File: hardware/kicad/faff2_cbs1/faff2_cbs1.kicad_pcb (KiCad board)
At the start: 4 copper layers, 210 x 130 mm, 412 parts, among them J1001 USB_C_Receptacle_USB2.0_16P, J1002 TSW-105-07-F-D, J1003 SAMTEC_SHF-107-01-L-D-SM, J1101 1x6 2.54mm, J1102 1x6 2.54mm, J1103 Micro-Fit 1x3, J201 KPJX-4S, J301 PH1-06-UA, J501 1729076, J502 8510-4500PL, J503 CONUFL001-SMD, J504 CONUFL001-SMD, J601 FH12-10S-0.5SH(55), J602 FTSH-105-01-L-DV-K-TR, J603 8510-4500PL, J701 1752120, J702 1752120, J703 8510-4500PL, J901 BTN EXT, J902 SMA Jack, J903 J-LIM, Q1101 BSZ099N06LS5, Q1102 BSZ099N06LS5, Q1103 BSZ099N06LS5, Q1104 BSZ099N06LS5, Q1105 BSZ099N06LS5, Q1106 BSZ099N06LS5, Q201 DMP6023LFG-7, SW1001 PTS526, SW901 PTS526, SW902 PTS526, SW903 PTS526, SW904 PTS526, U1001 STM32H723VET6, U1002 USB3320C, U1003 SRAM 32Mb, U1004 MIC5365-1.8, U1101 DRV8323S, U301 LMR33630, U302 ADPL42005, U303 ADPL42005, U304 LMR33630, U501 ADS1235, U601 AM26LV32, U701 ADS1120, U801 24FC16T-I/OT, U901 SN74LVC1G17, U902 SN74LVC1G11, Y1001 24MHz, Y1002 24MHz 18pF

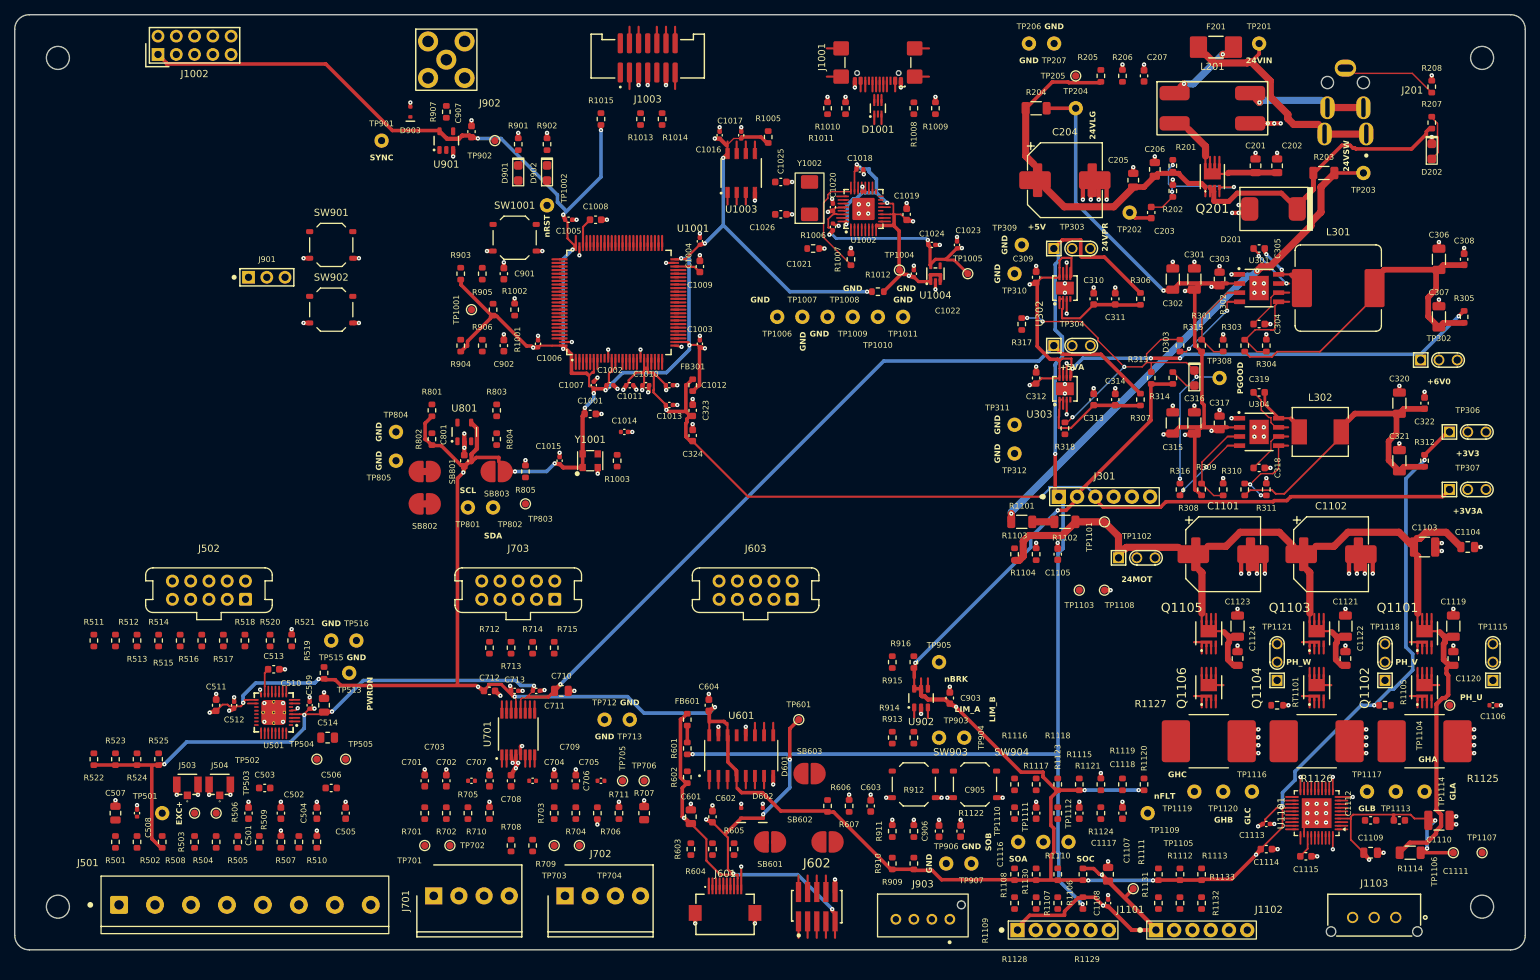
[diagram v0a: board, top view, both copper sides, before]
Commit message: pcb: routing step 4b/4c - via budget, and the three sealed pins (wip)
Step 4b: no power layer change may depend on too few barrels.  The test is
not how many vias a net has but how many it *depends* on -- a via whose
removal splits the net carries everything that crosses there -- so
`tools/route4b_powervias.py` searches every cut below the net's budget
(`ceil(I / 1.0 A)`, minimum 2 on a layer change) and parallels the vias it
names, tied on **both** outer layers, because two vias joined on one layer
only are in series through the other.  61 vias added over four passes;
`route_check.py --power` now returns ALL PROOFS PASS.

Step 4c (`tools/route4c_widen.py`, not yet run): the same argument for trace
width.  `connect_net`'s width ladder is right for the last hop onto a 0.5 mm
pad and wrong for a segment the whole rail crosses.

`tools/route_ripup.py`: windowed rip-up and reroute, for the three pins step 4
could not reach -- all three sealed in by another net's copper, which is the
R3-1 hazard.  Deletion runs in a child interpreter (Remove() poisons SWIG for
the rest of the process).  Two things had to be learned:

  * the pin-escape *reservation* is itself what seals a sealed pin -- leaving
    the package means crossing a neighbour's held lane at right angles, so
    U302 pin 7 routes in 14 mm with reservations off and not at all with them
    on; and the fan-out pass must not re-stub the ripped net's pins until the
    sealed net has its lane.
  * two adjacent pins that both have to leave the same way cannot both win on
    one layer.  U1101 pins 4/5 (VM and VDRAIN) cross layers instead; U302/U303
    PGOOD, the inner of its pair and a slow open-drain line, is the one that
    dives under the +6V0 approach.

U1101 pins 4 and 5 are done.  U302/U303 PGOOD are routed and the +6V0 tie is
mid-reroute -- banked here rather than held.

Also `tools/route7_stitch.py`, the G5 return-via pass, to run after the fill.

Co-Authored-By: Claude Opus 5 <noreply@anthropic.com>
Claude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
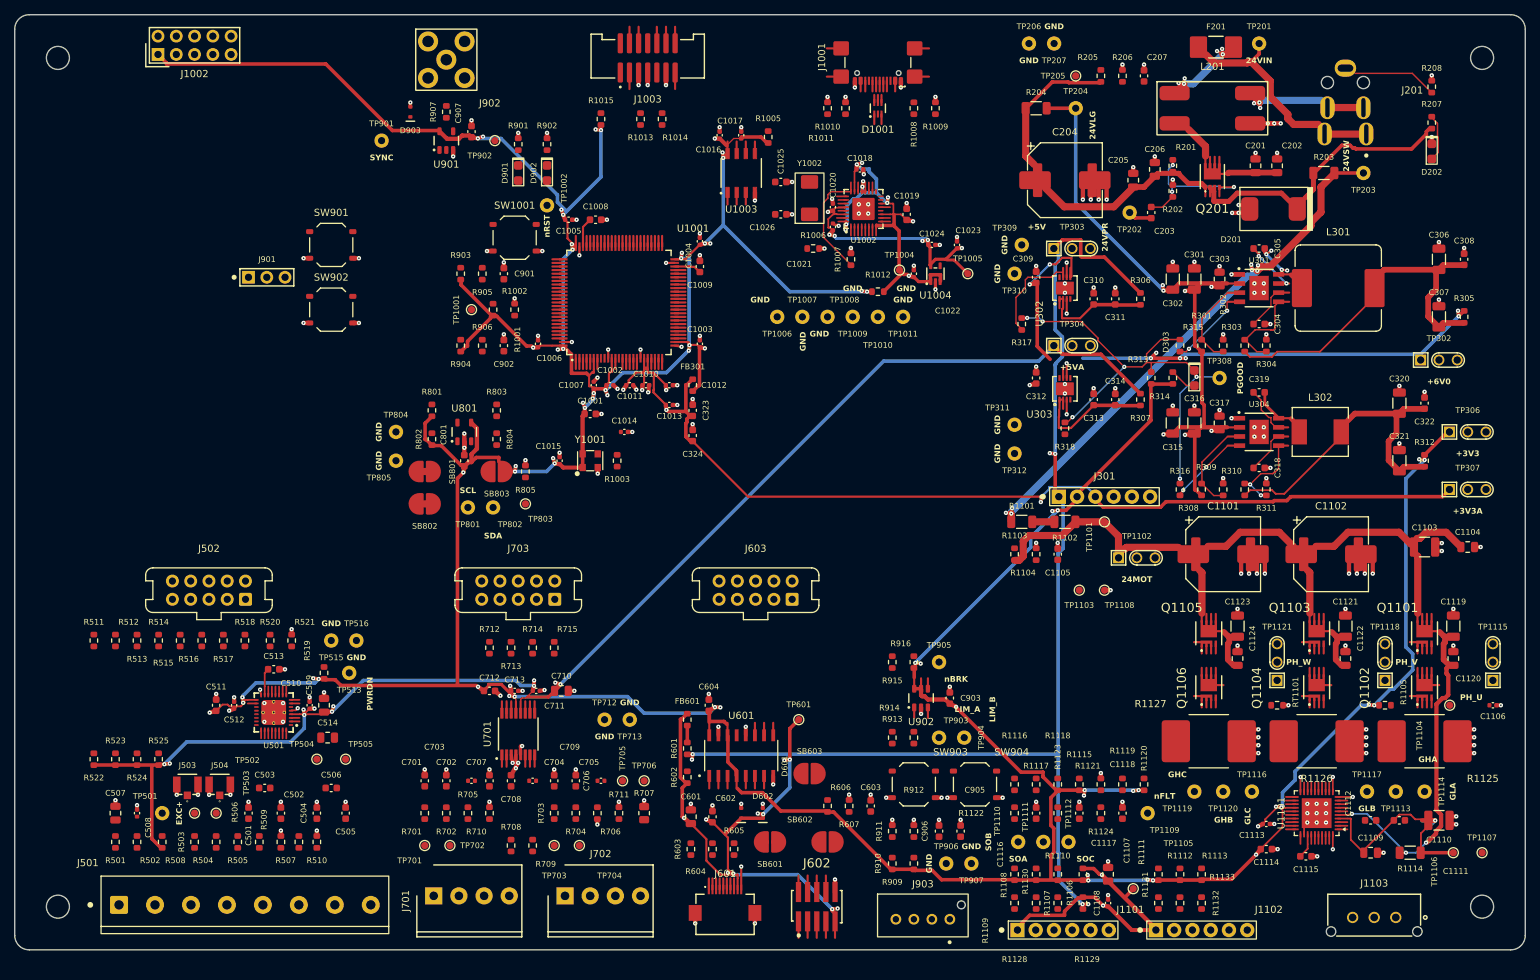
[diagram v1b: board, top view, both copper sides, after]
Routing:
- net +3V3: track 673.2 -> 715.5 mm, vias 39 -> 67
- net Net-(U302-PG): track 1.30 -> 14.7 mm
- net /power_rails/+6V0: track 95.8 -> 85.6 mm, vias 6 -> 9
- net /motor_drive/V24_MOT: track 158.5 -> 168.2 mm, vias 0 -> 3
- net /power_entry_24v/+24V_SW: track 71.9 -> 79.5 mm, vias 2 -> 7
- net +5VA: track 194.3 -> 201.8 mm, vias 6 -> 11
- net Net-(F201-Pad2): track 8.18 -> 14.6 mm, vias 2 -> 6
- net /linear_encoder/+5V_ENC: track 79.0 -> 85.1 mm, vias 6 -> 10
- net /mcu/+3V3_USB: track 54.4 -> 60.4 mm, vias 6 -> 10
- net +5V: track 163.2 -> 167.8 mm, vias 3 -> 6
- net Net-(U301-SW): track 6.45 -> 9.69 mm, vias 2 -> 4
- net /mcu/+1V8_USB: track 35.5 -> 38.5 mm, vias 4 -> 6
- net /power_entry_24v/V0_IN: track 12.7 -> 15.7 mm, vias 1 -> 3
- net +3V3A: track 144.1 -> 145.6 mm, vias 5 -> 6
- net /power_entry_24v/V24_LOGIC: track 91.0 -> 92.5 mm, vias 6 -> 7
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
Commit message: pcb: routing step 5 wip - fanout lanes and commutation pass A (inherited)
Banks the previous session's uncommitted step-5 progress before any further
edit, so the work is not lost: 638 segments and 88 vias on top of 9559620,
unconnected 390 -> 267.

Known defect carried in with it, fixed next: the USB HS pair reaches J1001
with DM and DP crossed over each other's pads, giving 9 shorting_items,
2 tracks_crossing, 3 clearance and 2 solder_mask_bridge violations, all
inside the 3 mm in front of the connector. Everything else DRC-clean beyond
the in-progress dangling stubs.

Co-Authored-By: Claude Opus 5 <noreply@anthropic.com>
Claude-Session: https://claude.ai/code/session_01WqUrajr7x5bwUMvjXpVkdq
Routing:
- net /motor_drive/MOTOR_V: track 13.4 -> 92.6 mm, vias 0 -> 5
- net /motor_drive/MOTOR_U: track 13.4 -> 86.9 mm, vias 0 -> 6
- net /motor_drive/MOTOR_W: track 13.4 -> 72.5 mm, vias 0 -> 4
- net Net-(U501B-REFN0): track 1.20 -> 50.0 mm, vias 0 -> 5
- net Net-(U501B-AIN0): track 1.20 -> 49.4 mm, vias 0 -> 2
- net Net-(U501B-AIN2): track 1.20 -> 48.9 mm, vias 0 -> 4
- net /linear_encoder/ENC_Z_N: track 5.58 -> 51.9 mm, vias 0 -> 3
- net Net-(J701-Pad3): track 0.00 -> 42.1 mm
- net /linear_encoder/ENC_VREF: track 0.00 -> 41.5 mm, vias 0 -> 5
- net /linear_encoder/ENC_A_N: track 5.58 -> 45.2 mm, vias 0 -> 3
- net /linear_encoder/ENC_B_N: track 5.58 -> 44.7 mm, vias 0 -> 4
- net Net-(J504-In): track 1.20 -> 38.8 mm, vias 0 -> 4
- net /linear_encoder/ENC_A_P: track 5.58 -> 41.6 mm, vias 0 -> 2
- net Net-(J503-In): track 1.20 -> 35.6 mm, vias 0 -> 2
- net Net-(U501B-REFP0): track 1.20 -> 34.9 mm, vias 0 -> 2
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
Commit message: pcb: routing step 5a - the USB HS pair, drawn rather than routed
Step 5 let the maze router loose on USB_DM/USB_DP.  With two pads per net in
one 0.5 mm row it treated them as interchangeable and ran DM along the pad
row through A6, a DP pad: nine shorting_items, two tracks_crossing, three
clearance and two solder_mask_bridge violations, all inside 3 mm of J1001.

A differential pair is a geometry specification, not a connectivity problem,
so tools/route9_usb.py draws it: explicit polylines, mirror images about
x = 150.0 wherever the two run together, so the match is by construction.
0.30 mm wide on 0.20 mm gap over In1.Cu = 90.6 ohm, F.Cu the whole through
path, no vias in either half.  Through-path length DM 15.71 / DP 16.13 mm,
skew 0.414 mm -- spent entirely on parting around D1001's pad-2 ground
stitch, which owns the lane south of the device.

What the geometry had to solve, for the captain's eye:

* J1001 interleaves the rows -- B6(DP) A7(DM) A6(DP) B7(DM) at 0.5 mm pitch
  -- so each B-row duplicate sits on the far side of the other net's lane and
  the two ties must cross.  0.5 mm pitch will not take a 0.6 mm via, so each
  descends its flank and crosses on B.Cu.  DP lands north of D1001; DM's band
  would have to cross both VBUS's spine and DP's band to do the same, so it
  lands 1.6 mm past pad 1 -- still 0.2 mm from a clamp cell of its own and
  9 mm ahead of the PHY.
* D1001 pin 5 is VBUS and its only escape is due north, between the two
  halves.  The pair opens to 1.4 mm pitch across the corridor so the via
  drops in with 0.25 mm each side; the bulge is symmetric and costs no skew.
* Nothing is routed under the connector on F.Cu: the shell lands there and
  soldermask is not an insulator under it.  The router went under twice
  before the reservation went in.
* CC2 walks the 0.60 mm gap between VBUS's via and the DP tie's at its own
  class width, 0.1524 -- a 0.30 mm trace needs 0.605 and does not fit.

route_check --usb now measures the *through pat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
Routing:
- net /mcu/USB_CC1: track 1.48 -> 16.1 mm, vias 0 -> 2
- net /mcu/USB_VBUS: track 4.00 -> 18.4 mm, vias 0 -> 3
- net /mcu/USB_CC2: track 1.48 -> 7.10 mm
- net /mcu/USB_DP: track 27.9 -> 25.0 mm
- net /mcu/USB_DM: track 28.0 -> 25.5 mm

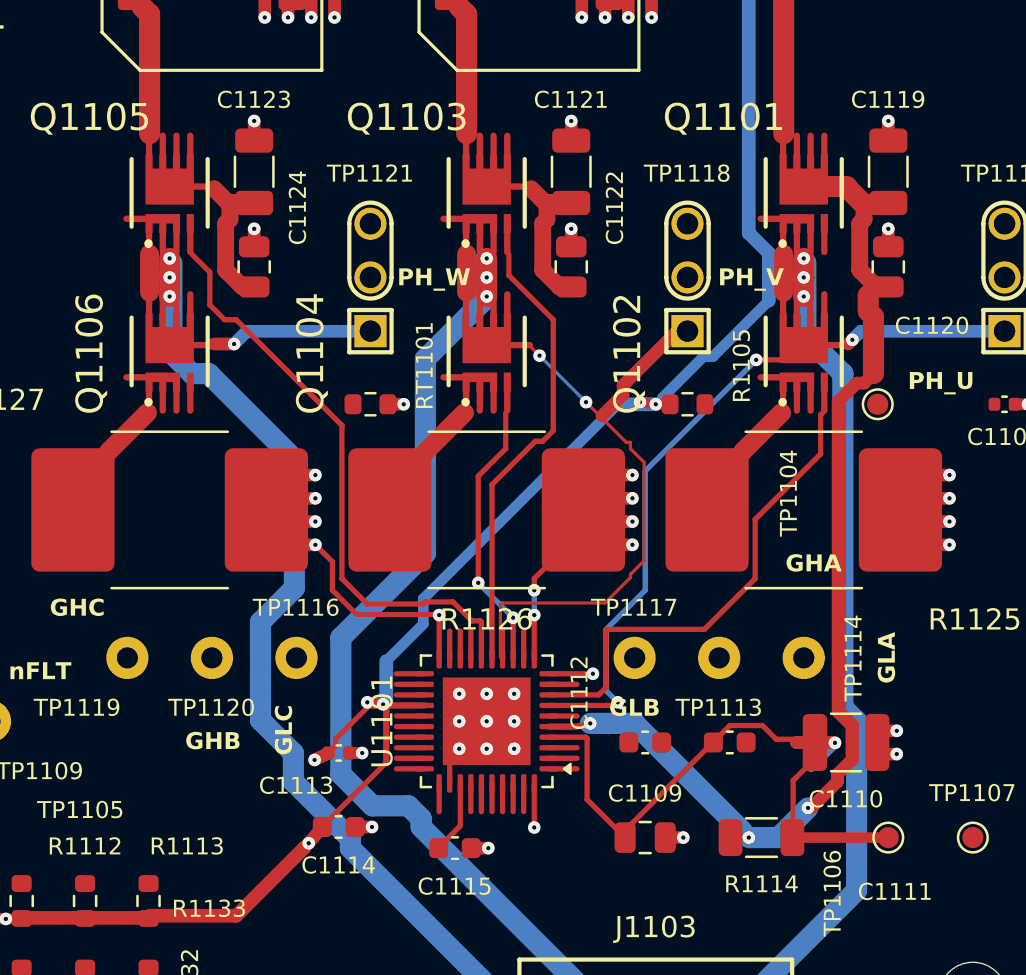
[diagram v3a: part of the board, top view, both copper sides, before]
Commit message: pcb: routing step 5b - the DRV8323 interface, accuracy before length
tools/route8_drv.py, run.  Fourteen nets have to reach one 6 mm package from
three legs spread over 30 mm, through a channel that also carries the motor
bus and the driver's own supply, and step 5's leg-by-leg order gave the
channel to whichever net asked first.  This rips the window and redoes it in
priority order.

Priority is accuracy, not length: the three Kelvin taps go first.  Each has
exactly one useful path -- from the shunt's own pad, never the power path --
and the CSA's gain error is whatever IR drop the tap picks up.  A gate run
that detours 4 mm costs nanoseconds of edge; a Kelvin tap that detours costs
percent of current-sense accuracy.  All three landed: SPA 8.89 mm, SPB
5.92 mm, SPC 21.74 mm.  V24_MOT is whole again at 1.00 mm.

Five of the six gates did not, and neither did VM_DRV's pin 4 -- see
docs/decisions/actuator-pcb-route1.md.  They are left for the general fill
with a fresh obstacle model rather than forced here, because the reason they
failed is that the taps legitimately took the channel first.

Unconnected 258 -> 254.  DRC severity-all 248: 199 track_dangling and 30
via_dangling (fan-out stubs) plus the 19 known library residuals.  Nothing
unexpected, schematic parity 0.

Co-Authored-By: Claude Opus 5 <noreply@anthropic.com>
Claude-Session: https://claude.ai/code/session_01WqUrajr7x5bwUMvjXpVkdq
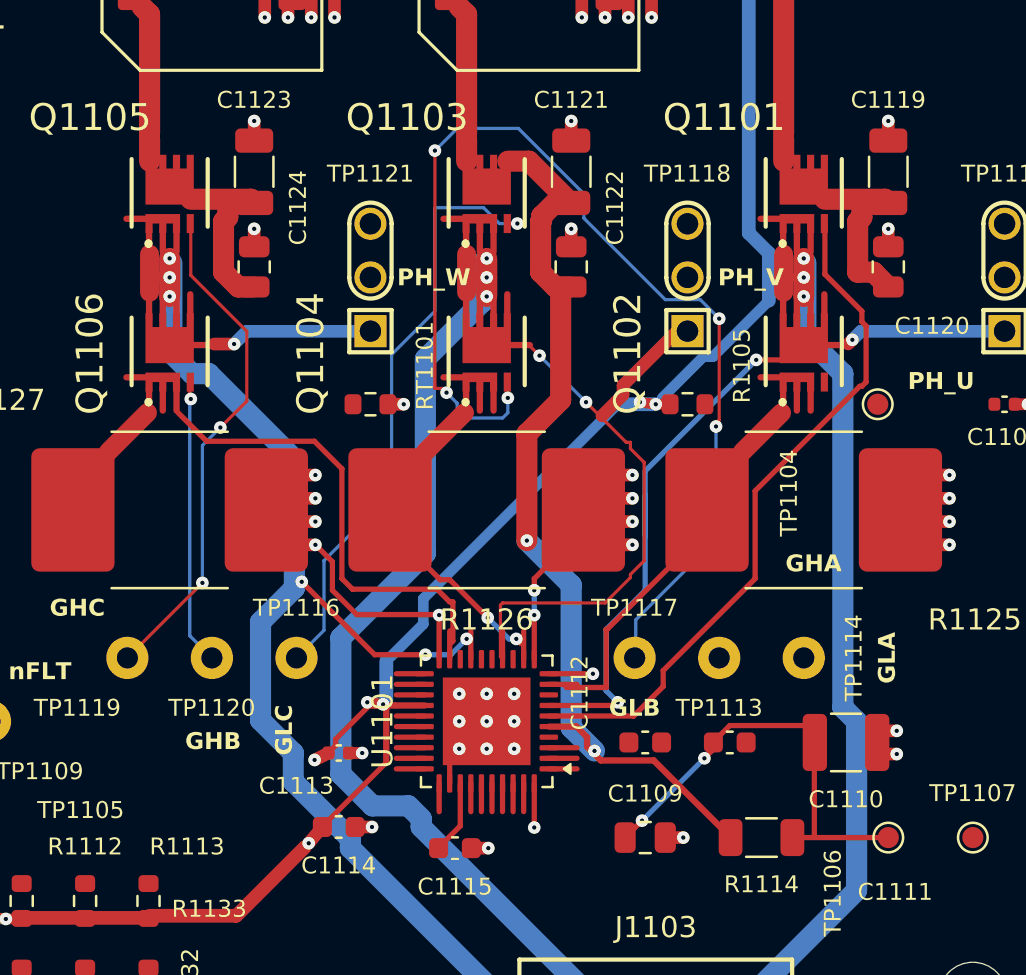
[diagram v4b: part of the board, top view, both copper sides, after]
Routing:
- net Net-(Q1104-G): track 14.2 -> 53.1 mm, vias 2 -> 5
- net Net-(Q1101-G): track 2.69 -> 32.7 mm
- net Net-(Q1102-G): track 24.1 -> 0.00 mm
- net Net-(Q1106-S_3): track 9.05 -> 30.8 mm
- net /motor_drive/V24_MOT: track 168.2 -> 147.9 mm, vias 3 -> 2
- net /motor_drive/MOTOR_W: track 72.5 -> 86.3 mm, vias 4 -> 7
- net /motor_drive/VM_DRV: track 31.3 -> 18.5 mm, vias 1 -> 2
- net Net-(Q1106-G): track 2.69 -> 13.4 mm, vias 0 -> 1
- net Net-(Q1102-S_3): track 9.05 -> 17.9 mm
- net Net-(Q1104-S_3): track 9.05 -> 15.0 mm, vias 0 -> 2
- net Net-(Q1103-G): track 22.7 -> 28.6 mm, vias 0 -> 1
- net Net-(Q1105-G): track 29.2 -> 23.9 mm, vias 0 -> 2
- net /motor_drive/MOTOR_U: track 86.9 -> 88.9 mm
